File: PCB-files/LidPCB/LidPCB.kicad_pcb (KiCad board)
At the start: 2 copper layers, 58 x 58 mm, 30 parts, among them J1 Conn_01x8_Female, U1 XC6206P332MR, U2 R1200N002A-TR-FE, U3 OLED-Display, U4 CAP1293-1-SN

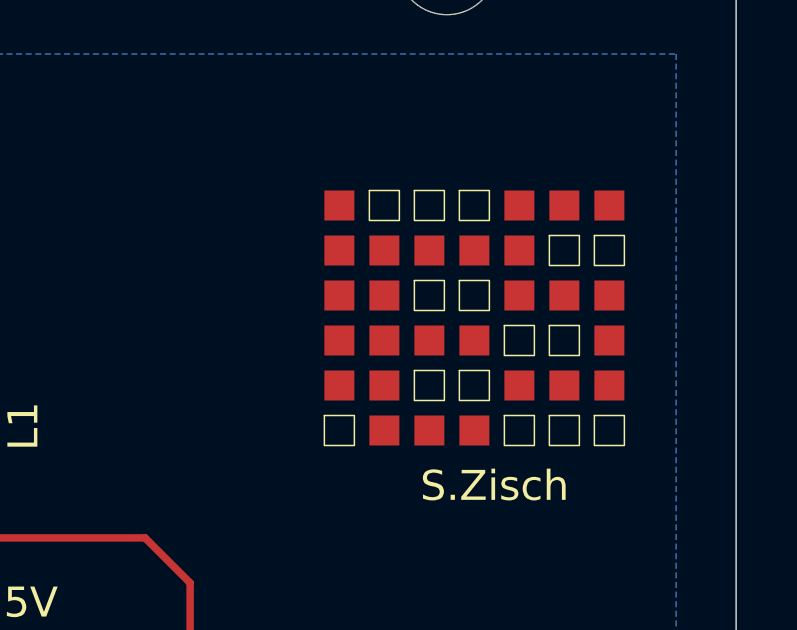
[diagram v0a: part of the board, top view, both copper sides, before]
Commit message: New SD Card PCB
In Altium designer, to use würth elektroniks lib
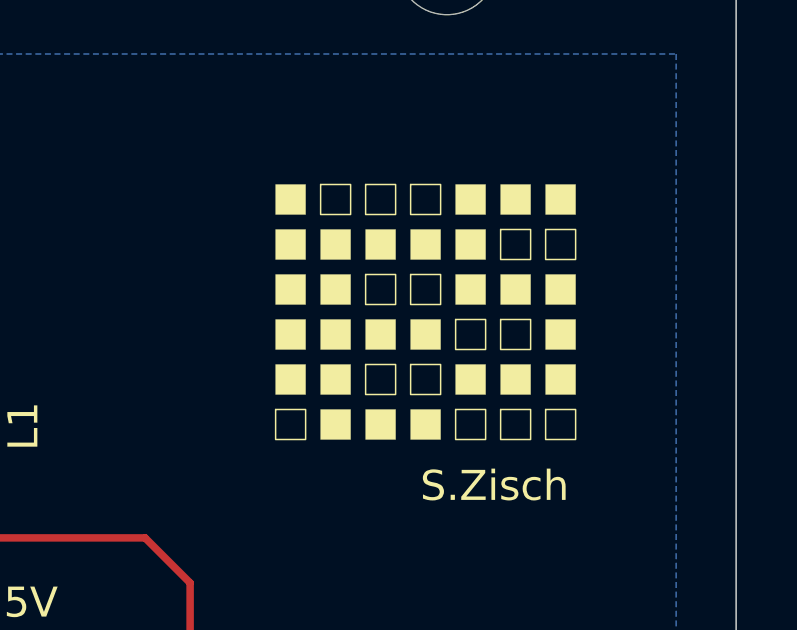
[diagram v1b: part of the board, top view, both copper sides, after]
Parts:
- removed the REF** at (159.3, 70.5)
- added REF**: IES_Logo, IES-Logo:IES_Logo, F.Cu at (157.7, 70.3)
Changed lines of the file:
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@@
       (net 5 "+5V"))
+  )
+  (footprint "IES-Logo:IES_Logo" (layer "F.Cu")
+    (at 157.65 70.35)
+    (attr smd)
+    (fp_text reference "REF**" (at 4.15 -1.42 unlocked) (layer "F.SilkS") hide
+      (effects (font (size 1 1) (thickness 0.15)))
+    )
+    (fp_text value "IES_Logo" (at 4.15 0.08 unlocked) (layer "F.Fab")
+      (effects (font (size 1 1) (thickness 0.15)))
+    )
+    (fp_rect (start 3 6.5) (end 4 7.5) (layer "F.SilkS") (width 0.05) (fill none))
+    (fp_rect (start 1.5 10.5) (end 2.5 9.5) (layer "F.SilkS") (width 0.01) (fill solid))
+    (fp_rect (start 1.5 2) (end 2.5 3) (layer "F.SilkS") (width 0.05) (fill none))
+    (fp_rect (start 6 3.5) (end 7 4.5) (layer "F.SilkS") (width 0.05) (fill none))
+    (fp_rect (start 0 2) (end 1 3) (layer "F.SilkS") (width 0.05) (fill none))
+    (fp_rect (start -1.5 4.5) (end -0.5 3.5) (layer "F.SilkS") (width 0.01) (fill solid))
+    (fp_rect (start 4.5 9) (end 5.5 8) (layer "F.SilkS") (width 0.01) (fill solid))
+    (fp_rect (start 0 10.5) (end 1 9.5) (layer "F.SilkS") (width 0.01) (fill solid))
+    (fp_rect (start -1.5 6.5) (end -0.5 7.5) (layer "F.SilkS") (width 0.01) (fill solid))
+    (fp_rect (start 4.5 6.5) (end 5.5 7.5) (layer "F.SilkS") (width 0.05) (fill none))
+    (fp_rect (start 4.5 3) (end 5.5 2) (layer "F.SilkS") (width 0.01) (fill solid))
+    (fp_rect (start 6 9) (end 7 8) (layer "F.SilkS") (width 0.01) (fill solid))
+    (fp_rect (start 6 6.5) (end 7 7.5) (layer "F.SilkS") (width 0.01) (fill solid))
+    (fp_rect (start 0 8) (end 1 9) (layer "F.SilkS") (width 0.05) (fill none))
+    (fp_rect (start 1.5 4.5) (end 2.5 3.5) (layer "F.SilkS") (width 0.01) (fill solid))
+    (fp_rect (start 0 5) (end 1 6) (layer "F.SilkS") (width 0.05) (fill none))
+    (fp_rect (start 3 2) (end 4 3) (layer "F.SilkS") (width 0.01) (fill solid))
+    (fp_rect (start 1.5 8) (end 2.5 9) (layer "F.SilkS") (width 0.05) (fill none))
+    (fp_rect (start 6 5) (end 7 6) (layer "F.SilkS") (width 0.01) (fill solid))
+    (fp_rect (start 4.5 3.5) (end 5.5 4.5) (layer "F.SilkS") (width 0.05) (fill none))
+    (fp_rect (start -3 6.5) (end -2 7.5) (layer "F.SilkS") (width 0.01) (fill solid))
+    (fp_rect (start 6 3) (end 7 2) (layer "F.SilkS") (width 0.01) (fill solid))
+    (fp_rect (start -1.5 2) (end -0.5 3) (layer "F.SilkS") (width 0.05) (fill none))
+    (fp_rect (start 6 9.5) (end 7 10.5) (layer "F.SilkS") (width 0.05) (fill none))
+    (fp_rect (start 1.5 5) (end 2.5 6) (layer "F.SilkS") (width 0.05) (fill none))
+    (fp_rect (start -1.5 9) (end -0.5 8) (layer "F.SilkS") (width 0.01) (fill solid))
+    (fp_rect (start 4.5 9.5) (end 5.5 10.5) (layer "F.SilkS") (width 0.05) (fill none))
+    (fp_rect (start 3 3.5) (end 4 4.5) (layer "F.SilkS") (width 0.01) (fill solid))
+    (fp_rect (start -3 9.5) (end -2 10.5) (layer "F.SilkS") (width 0.05) (fill none))
+    (fp_rect (start -3 5) (end -2 6) (layer "F.SilkS") (width 0.01) (fill solid))
+    (fp_rect (start 0 7.5) (end 1 6.5) (layer "F.SilkS") (width 0.01) (fill solid))
+    (fp_rect (start 0 4.5) (end 1 3.5) (layer "F.SilkS") (width 0.01) (fill solid))
+    (fp_rect (start 3 6) (end 4 5) (layer "F.SilkS") (width 0.01) (fill solid))
+    (fp_rect (start -3 9) (end -2 8) (layer "F.SilkS") (width 0.01) (fill solid))
+    (fp_rect (start -1.5 5) (end -0.5 6) (layer "F.SilkS") (width 0.01) (fill solid))
+    (fp_rect (start 3 9) (end 4 8) (layer "F.SilkS") (width 0.01) (fill solid))
+    (fp_rect (start -3 2) (end -2 3) (layer "F.SilkS") (width 0.01) (fill solid))
+    (fp_rect (start 3 9.5) (end 4 10.5) (layer "F.SilkS") (width 0.05) (fill none))
+    (fp_rect (start -1.5 10.5) (end -0.5 9.5) (layer "F.SilkS") (width 0.01) (fill solid))
+    (fp_rect (start 4.5 6) (end 5.5 5) (layer "F.SilkS") (width 0.01) (fill solid))
+    (fp_rect (start 1.5 7.5) (end 2.5 6.5) (layer "F.SilkS") (width 0.01) (fill solid))
+    (fp_rect (start -3 3.5) (end -2 4.5) (layer "F.SilkS") (width 0.01) (fill solid))
   )
   (footprint "TestPoint:TestPoint_Pad_D2.0mm" (layer "F.Cu")
@@
       (net 2 "GND"))
   )
-  (footprint "IES_Logo:IES_Logo" (layer "F.Cu")
-    (at 159.275 70.55)
-    (attr smd)
-    (fp_text reference "REF**" (at 4.15 -1.42 unlocked) (layer "F.SilkS") hide
-      (effects (font (size 1 1) (thickness 0.15)))
-    )
-    (fp_text value "IES_Logo" (at 4.15 0.08 unlocked) (layer "F.Fab")
-      (effects (font (size 1 1) (thickness 0.15)))
-    )
-    (fp_rect (start 1.5 8) (end 2.5 9) (layer "F.SilkS") (width 0.05) (fill none))
-    (fp_rect (start -3 9.5) (end -2 10.5) (layer "F.SilkS") (width 0.05) (fill none))
-    (fp_rect (start 1.5 2) (end 2.5 3) (layer "F.SilkS") (width 0.05) (fill none))
-    (fp_rect (start 0 2) (end 1 3) (layer "F.SilkS") (width 0.05) (fill none))
-    (fp_rect (start 4.5 9.5) (end 5.5 10.5) (layer "F.SilkS") (width 0.05) (fill none))
-    (fp_rect (start 4.5 3.5) (end 5.5 4.5) (layer "F.SilkS") (width 0.05) (fill none))
-    (fp_rect (start -1.5 2) (end -0.5 3) (layer "F.SilkS") (width 0.05) (fill none))
-    (fp_rect (start 6 3.5) (end 7 4.5) (layer "F.SilkS") (width 0.05) (fill none))
-    (fp_rect (start 4.5 6.5) (end 5.5 7.5) (layer "F.SilkS") (width 0.05) (fill none))
-    (fp_rect (start 3 9.5) (end 4 10.5) (layer "F.SilkS") (width 0.05) (fill none))
-    (fp_rect (start 1.5 5) (end 2.5 6) (layer "F.SilkS") (width 0.05) (fill none))
-    (fp_rect (start 6 9.5) (end 7 10.5) (layer "F.SilkS") (width 0.05) (fill none))
-    (fp_rect (start 0 5) (end 1 6) (layer "F.SilkS") (width 0.05) (fill none))
-    (fp_rect (start 0 8) (end 1 9) (layer "F.SilkS") (width 0.05) (fill none))
-    (fp_rect (start 3 6.5) (end 4 7.5) (layer "F.SilkS") (width 0.05) (fill none))
-    (pad "1" smd rect (at -2.5 2.5) (size 1 1) (layers "F.Cu" "F.Paste" "F.Mask"))
-    (pad "5" smd rect (at 3.5 2.5) (size 1 1) (layers "F.Cu" "F.Paste" "F.Mask"))
-    (pad "6" smd rect (at 5 2.5) (size 1 1) (layers "F.Cu" "F.Paste" "F.Mask"))
-    (pad "7" smd rect (at 6.5 2.5) (size 1 1) (layers "F.Cu" "F.Paste" "F.Mask"))
-    (pad "8" smd rect (at -2.5 4) (size 1 1) (layers "F.Cu" "F.Paste" "F.Mask"))
-    (pad "9" smd rect (at -1 4) (size 1 1) (layers "F.Cu" "F.Paste" "F.Mask"))
-    (pad "10" smd rect (at 0.5 4) (size 1 1) (layers "F.Cu" "F.Paste" "F.Mask"))
-    (pad "11" smd rect (at 2 4) (size 1 1) (layers "F.Cu" "F.Paste" "F.Mask"))
-    (pad "12" smd rect (at 3.5 4) (size 1 1) (layers "F.Cu" "F.Paste" "F.Mask"))
-    (pad "15" smd rect (at -2.5 5.5) (size 1 1) (layers "F.Cu" "F.Paste" "F.Mask"))
-    (pad "16" smd rect (at -1 5.5) (size 1 1) (layers "F.Cu" "F.Paste" "F.Mask"))
-    (pad "19" smd rect (at 3.5 5.5) (size 1 1) (layers "F.Cu" "F.Paste" "F.Mask"))
-    (pad "20" smd rect (at 5 5.5) (size 1 1) (layers "F.Cu" "F.Paste" "F.Mask"))
-    (pad "21" smd rect (at 6.5 5.5) (size 1 1) (layers "F.Cu" "F.Paste" "F.Mask"))
-    (pad "22" smd rect (at -2.5 7) (size 1 1) (layers "F.Cu" "F.Paste" "F.Mask"))
-    (pad "23" smd rect (at -1 7) (size 1 1) (layers "F.Cu" "F.Paste" "F.Mask"))
-    (pad "24" smd rect (at 0.5 7) (size 1 1) (layers "F.Cu" "F.Paste" "F.Mask"))
-    (pad "25" smd rect (at 2 7) (size 1 1) (layers "F.Cu" "F.Paste" "F.Mask"))
-    (pad "28" smd rect (at 6.5 7) (size 1 1) (layers "F.Cu" "F.Paste" "F.Mask"))
-    (pad "29" smd rect (at -2.5 8.5) (size 1 1) (layers "F.Cu" "F.Paste" "F.Mask"))
-    (pad "30" smd rect (at -1 8.5) (size 1 1) (layers "F.Cu" "F.Paste" "F.Mask"))
-    (pad "33" smd rect (at 3.5 8.5) (size 1 1) (layers "F.Cu" "F.Paste" "F.Mask"))
-    (pad "34" smd rect (at 5 8.5) (size 1 1) (layers "F.Cu" "F.Paste" "F.Mask"))
-    (pad "35" smd rect (at 6.5 8.5) (size 1 1) (layers "F.Cu" "F.Paste" "F.Mask"))
-    (pad "37" smd rect (at -1 10) (size 1 1) (layers "F.Cu" "F.Paste" "F.Mask"))
-    (pad "38" smd rect (at 0.5 10) (size 1 1) (layers "F.Cu" "F.Paste" "F.Mask"))
-    (pad "39" smd rect (at 2 10) (size 1 1) (layers "F.Cu" "F.Paste" "F.Mask"))
-  )
   (footprint "TestPoint:TestPoint_Pad_D2.0mm" (layer "F.Cu")
